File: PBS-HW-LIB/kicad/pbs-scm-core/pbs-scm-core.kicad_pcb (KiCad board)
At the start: 4 copper layers, 92 x 92 mm, 51 parts, among them J1 Host connector, blind-mate, s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, J2 Coaxial antenna port: cellular, J3 Coaxial antenna port: 2.4 GHz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, J4 Coaxial antenna port: S-band 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, J5 Coaxial antenna port: navigat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, J6 Coaxial antenna port: UWB, Q1 Heater driver, low-side MOSFET, SW1 Release-request switch (latch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, U1 Input TVS and EMI filter, U10 Current-limited load switch (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, U11 Current-limited load switch (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, U12 Current-limited load switch (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, U13 Radiation-hardened microcontr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, U14 Radiation-tolerant NOR flash 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, U15 Store-and-forward memory, at 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, U16 Single-pair Ethernet PHY (100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, U17 RS-422 transceiver, U18 Hot-swap I2C bus buffer with 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, U19 LTE/NR modem module (3GPP dev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, U2 Hot-swap controller with inru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, U20 eSIM (MFF2), U21 Wi-Fi SoC with 802.11s mesh (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, U22 Wideband SDR transceiver RFIC, U23 Low-power FPGA (waveform proc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, U24 S-band power amplifier, 2 W, U25 S-band front end: T/R switch 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, U26 RF antenna selector switch (l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, U27 UWB ranging transceiver (opti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, U3 Swap-detect conditioning (com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, U4 Hold-up controller (ideal dio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, U5 Wide-input DC-DC buck convert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, U6 Point-of-load regulators (3.3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, U7 Voltage supervisor with watch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, U8 Current-limited load switch (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, U9 Current-limited load switch (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, Y1 TCXO reference oscillator

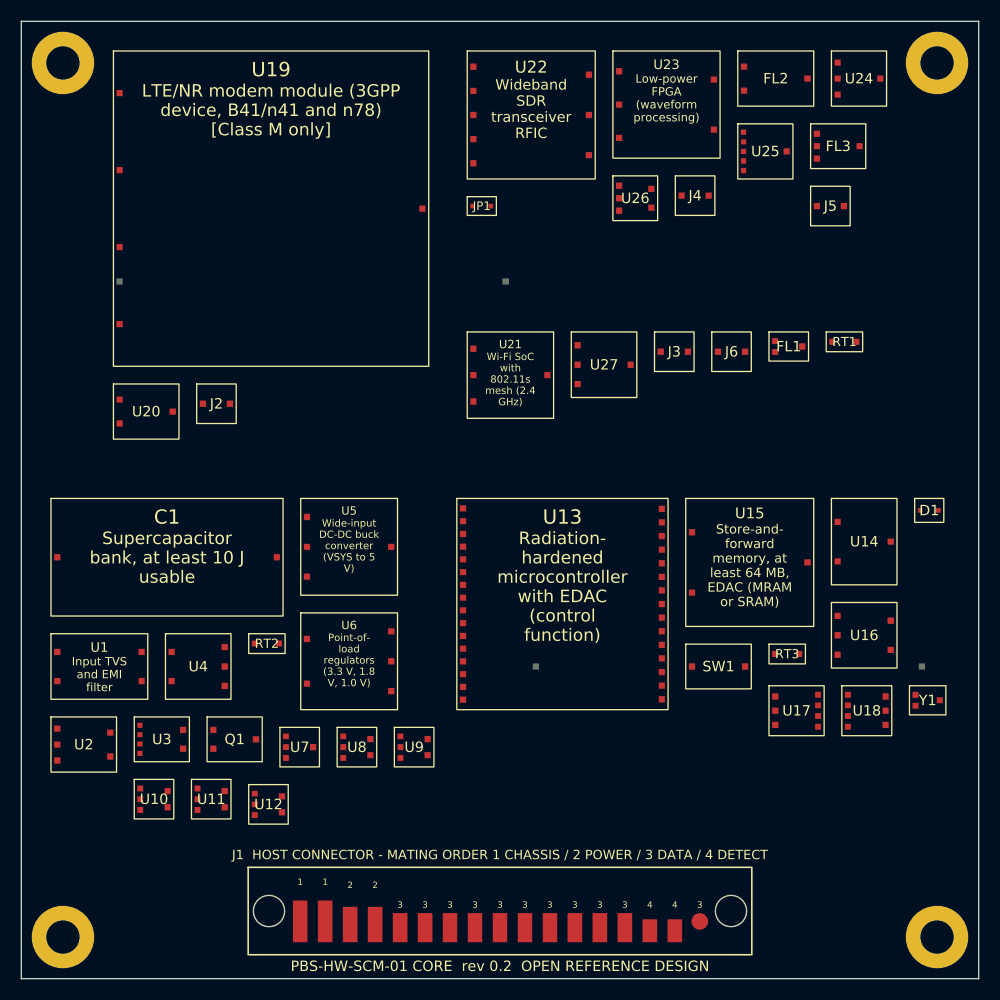
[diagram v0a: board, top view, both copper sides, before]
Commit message: Define the module host connector (PBS-HW-CON-01)
Add PBS-HW-CON-01: a face-to-face blind-mate connector with 17 contacts at
stated positions, flat pads on the module and spring contacts in the bay,
mating order set by four free heights 0.60 mm apart, keyed guide pins
(A 4.00, B 3.00), a bay cover plate and covered module apertures, an SMP
RF contact, forces and electrical ratings. Two dimensioned drawing sheets.

KiCad: both J1 footprints now follow the contact map (module half on the
back of the core board, centred; bay half with spring-contact holes and
guide pins), with 3D models showing contact heights, guide pins and the
cover plate. All geometry comes from tools/connector.py.

PBS-HW-SCM-01 v0.3 references the connector document.
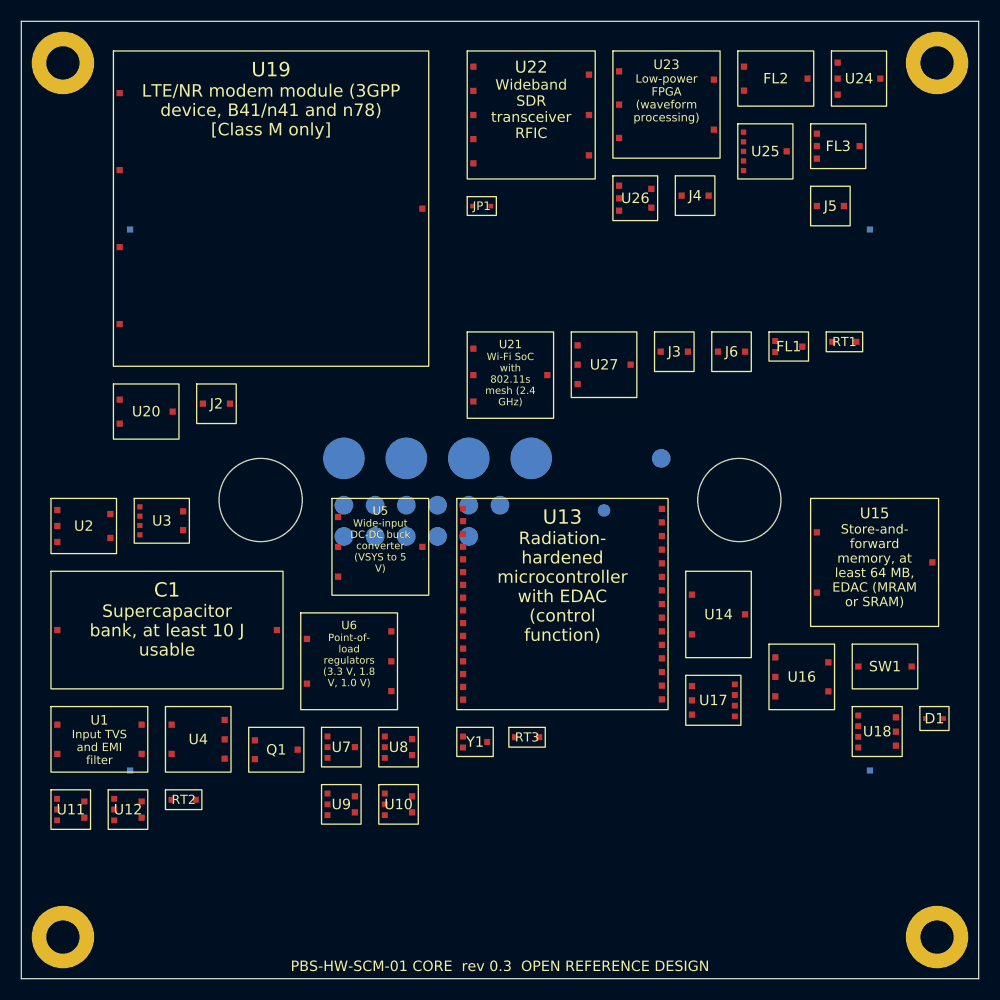
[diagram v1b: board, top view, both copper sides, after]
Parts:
- J1: value Host connector, blind-mate, shuttered (PBS-HW-SCM-01 Section 5.2) -> Host connector, module half: contact pads and guide bushings (PBS-HW-CON-01); footprint PBS_Generic:J1_Host_connector_blind_mate_shuttered_PBS_HW_SCM_01_Section_5_2 -> PBS_Generic:J1_Host_connector_module_half_contact_pads_and_guide_bushings_PBS_HW_CON_01; moved to B.Cu
- moved Y1 43.7 mm to (93.6, 119.2)
- moved J1 39.5 mm to (96.0, 96.0), turned to 180 degrees
- moved RT3 26.2 mm to (98.6, 118.8)
- moved H2 24.2 mm to (96.0, 122.0)
- moved U10 23.5 mm to (86.2, 125.2)
- moved U2 21.0 mm to (56.0, 98.5)
- moved U3 21.0 mm to (63.5, 98.0)
- moved D1 20.0 mm to (137.8, 117.0)
- moved H1 18.7 mm to (96.0, 70.0)
- moved RT2 17.0 mm to (65.6, 124.8)
- moved SW1 16.0 mm to (133.0, 112.0)
- moved U14 15.7 mm to (117.0, 107.0)
- moved U11 13.5 mm to (54.8, 125.8)
- moved U12 13.5 mm to (60.2, 125.8)
- moved U15 12.0 mm to (132.0, 102.0)
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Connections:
- J1 pad 10: RS422_RX_N -> GND
- J1 pad 11: ID_3V3 -> DET_A
- J1 pad 12: GND -> TX+
- J1 pad 13: ID_SCL -> TX-
- J1 pad 14: ID_SDA -> RX+
- J1 pad 15: DET_A -> RX-
- J1 pad 2: CHASSIS -> GND
- J1 pad 4: GND -> CHASSIS
- J1 pad 7: RS422_TX_P -> ID_3V3
- J1 pad 8: RS422_TX_N -> ID_SCL
- J1 pad 9: RS422_RX_P -> ID_SDA
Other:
- board text added: "J1 Host connector, module half: contact pads and guide bushings (PBS-HW-CON-01) (back)"
- board text added: "PBS-HW-SCM-01 CORE rev 0.3 OPEN REFERENCE DESIGN"
- board text removed: "J1 Host connector, blind-mate, shuttered (PBS-HW-SCM-01 Section 5.2)"
- board text removed: "PBS-HW-SCM-01 CORE rev 0.2 OPEN REFERENCE DESIGN"
